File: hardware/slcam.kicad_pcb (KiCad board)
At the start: 4 copper layers, 42.2 x 25.4 mm, 34 parts, among them J1 532610671, J2 Conn_01x08, J3 Conn_01x04, J4 532610371, J5 532610371, U1 STM32F103C8Tx, U2 W25Q128JVS, U3 TCAN330G, U4 TPS2044D, Y1 Crystal_GND24

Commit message: hardware: finishing fixes and new components
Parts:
- added C10: 12pF, Capacitor_SMD:C_0603_1608Metric_Pad1.08x0.95mm_HandSolder, B.Cu at (234.1, 64.8)
- added C9: 12pF, Capacitor_SMD:C_0603_1608Metric_Pad1.08x0.95mm_HandSolder, B.Cu at (234.1, 62.6)
- added Y2: Crystal, lib:ECS-.327-12.5-34R-C-TR, B.Cu at (231.0, 63.7)
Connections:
- J1 pad 3: /SPI_MOSI -> /SPI_MISO
- J1 pad 4: /SPI_MISO -> /SPI2_MOSI
- J2 pad 2: /SPI_MOSI -> /SPI2_MOSI
- J2 pad 3: /SPI_MISO -> /SPI2_MISO
- J2 pad 4: /SPI_SCK -> /SPI2_SCK
- U1 pad 13: /SPI_NSS_FLASH -> unconnected-(U1-Pad13)
- U1 pad 23: unconnected-(U1-Pad23) -> GND
- U1 pad 25: unconnected-(U1-Pad25) -> /SPI_NSS_FLASH
- U1 pad 26: unconnected-(U1-Pad26) -> /SPI2_SCK
- U1 pad 27: unconnected-(U1-Pad27) -> /SPI2_MISO
- U1 pad 28: unconnected-(U1-Pad28) -> /SPI2_MOSI
- U1 pad 3: unconnected-(U1-Pad3) -> /OSC_IN2
- U1 pad 35: unconnected-(U1-Pad35) -> GND
- U1 pad 4: unconnected-(U1-Pad4) -> /OSC_OUT2
- U1 pad 40: unconnected-(U1-Pad40) -> /CAN_SHDN
- U1 pad 41: unconnected-(U1-Pad41) -> /CAN_S
- U1 pad 45: unconnected-(U1-Pad45) -> /FLASH_WP
- U1 pad 46: unconnected-(U1-Pad46) -> /FLASH_HR
- U1 pad 47: unconnected-(U1-Pad47) -> GND
- U1 pad 8: unconnected-(U1-Pad8) -> GND
- U2 pad 2: /SPI_MOSI -> /SPI2_MISO
- U2 pad 3: unconnected-(U2-Pad3) -> /FLASH_HR
- U2 pad 5: /SPI_MISO -> /SPI2_MOSI
- U2 pad 6: /SPI_SCK -> /SPI2_SCK
- U2 pad 7: unconnected-(U2-Pad7) -> /FLASH_WP
- U3 pad 5: unconnected-(U3-Pad5) -> /CAN_SHDN
- U3 pad 8: unconnected-(U3-Pad8) -> /CAN_S
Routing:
- net /SPI_MOSI: track 67.5 -> 0.00 mm, vias 1 -> 0
- net /SPI2_MISO: track 0.00 -> 62.9 mm
- net /SPI_MISO: track 63.1 -> 5.41 mm, vias 2 -> 1
- net /SPI_SCK: track 66.7 -> 12.0 mm, vias 3 -> 1
- net /SPI2_MOSI: track 0.00 -> 47.0 mm, vias 0 -> 3
- net /SPI2_SCK: track 0.00 -> 32.7 mm, vias 0 -> 2
- net GND: track 148.2 -> 170.0 mm, vias 13 -> 14
- net /CAN_S: track 0.00 -> 20.2 mm, vias 0 -> 2
- net /CAN_SHDN: track 0.00 -> 16.3 mm, vias 0 -> 2
- net /OSC_OUT2: track 0.00 -> 16.0 mm, vias 0 -> 2
- net /FLASH_HR: track 0.00 -> 15.6 mm, vias 0 -> 2
- net /OSC_IN2: track 0.00 -> 13.7 mm, vias 0 -> 2
- net /SPI_NSS_FLASH: track 23.7 -> 37.3 mm, vias 1 -> 2
- net /FLASH_WP: track 0.00 -> 11.2 mm, vias 0 -> 2
- net VCC: track 111.6 -> 114.6 mm
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
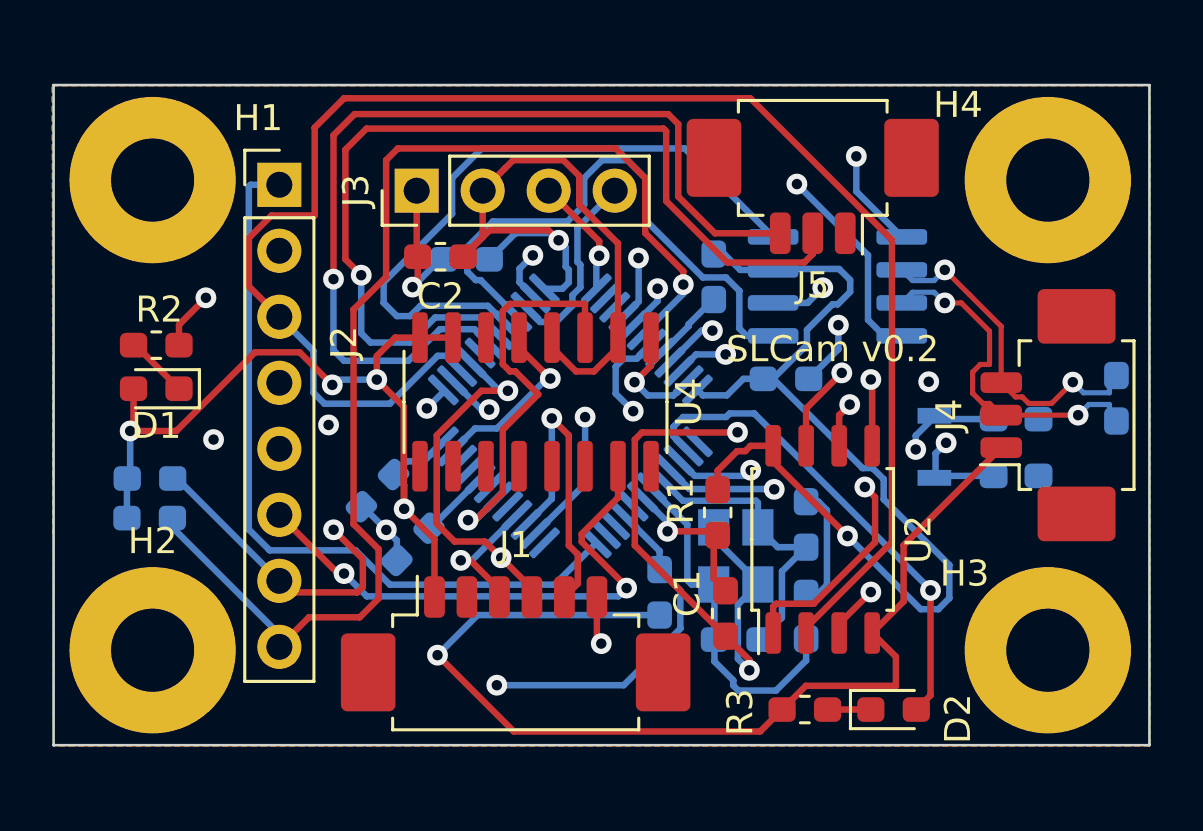
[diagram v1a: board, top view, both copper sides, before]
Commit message: hardware: Fixing DRC errors and general improvements in the layout
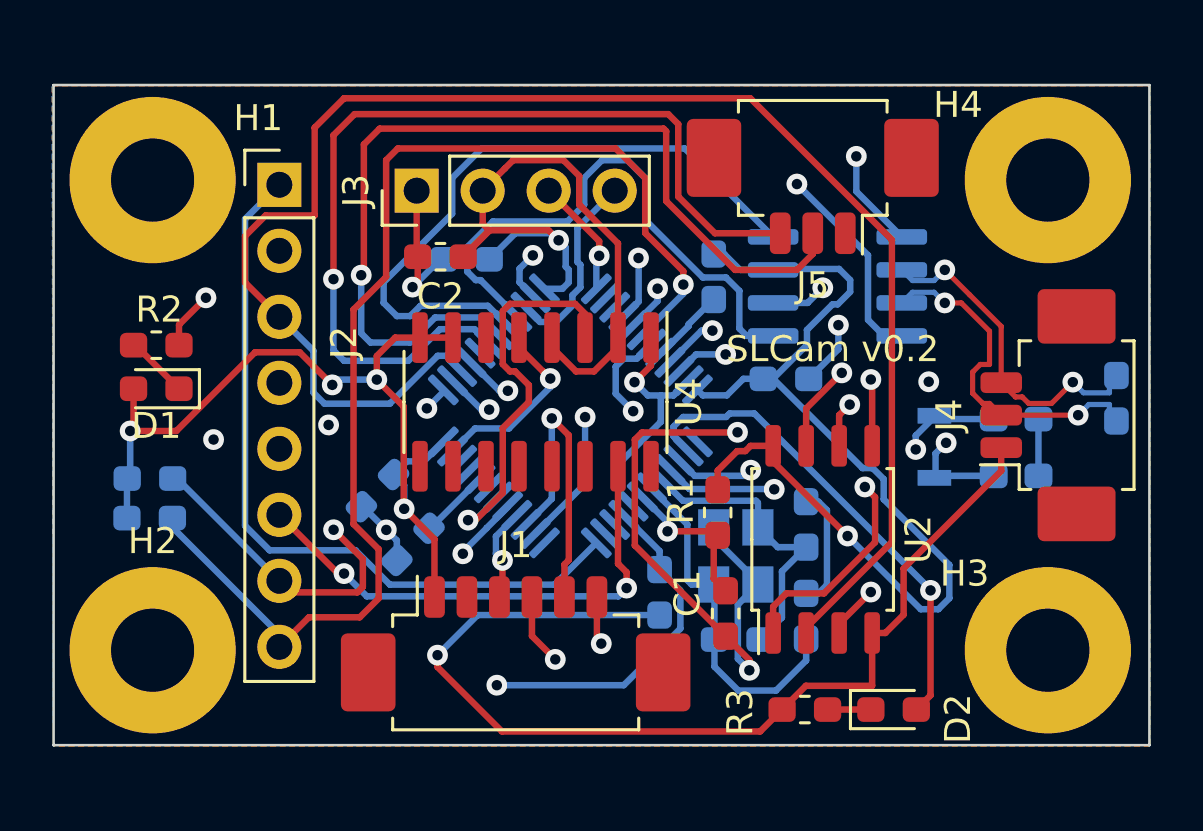
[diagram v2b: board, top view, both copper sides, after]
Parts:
- moved G*** 21.9 mm to (214.1, 72.4), turned to 180 degrees
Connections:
- J1 pad 4: /SPI2_MOSI -> /SPI_MOSI
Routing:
- net /SPI2_MOSI: track 47.0 -> 35.2 mm, vias 3 -> 2
- net /SPI_MOSI: track 0.00 -> 10.9 mm, vias 0 -> 2
- net GND: track 170.0 -> 177.0 mm
- net /SPI_MISO: track 5.41 -> 3.63 mm
- net /3V3_IMG_SENSOR: track 20.9 -> 19.7 mm
- net /SPI2_MISO: track 62.9 -> 61.8 mm
- net /UART_RX: track 36.4 -> 35.8 mm
- net /EN_SWITCH: track 16.1 -> 15.6 mm
- net /SPI_NSS_IMG: track 29.3 -> 28.8 mm

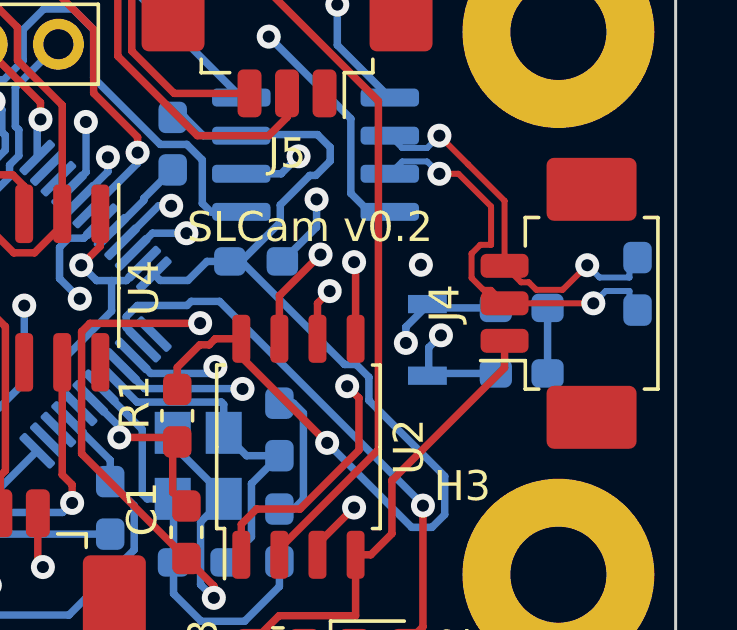
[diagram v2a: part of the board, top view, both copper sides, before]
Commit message: hardware: Fixing the footprint of the 32 kHz crystal #45
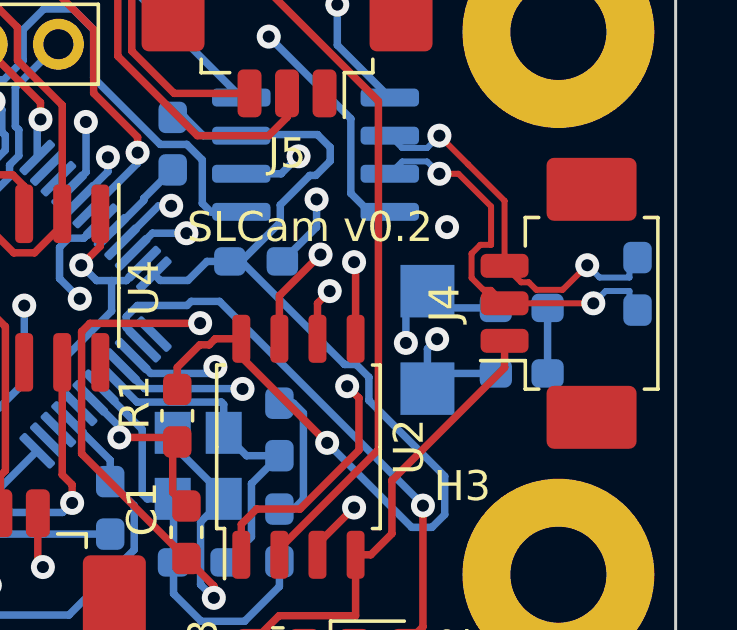
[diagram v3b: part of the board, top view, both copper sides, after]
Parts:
- Y2: footprint lib:ECS-.327-12.5-34R-C-TR -> Crystal:Crystal_SMD_MicroCrystal_CC7V-T1A-2Pin_3.2x1.5mm_HandSoldering
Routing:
- net /OSC_IN2: track 13.7 -> 14.3 mm

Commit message: hardware: changing component values #52
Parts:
- D1: value LED -> SMD Green LED
- D2: value LED -> SMD Orange LED
- U1: value STM32F103C8Tx -> STM32F103C8T6
- U3: value TCAN330G -> TCAN330GD
- U4: value TPS2044D -> TPS2010AD
- Y1: value Crystal_GND24 -> ECS-80-10-33-CHN-TR3
- Y2: value Crystal -> ECS-.327-12.5-34S-TR
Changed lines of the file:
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@@
       (effects (font (size 1 1) (thickness 0.15)))
     )
-    (fp_text value "TPS2044D" (at 0 5.9 90) (layer "F.Fab")
+    (fp_text value "TPS2010AD" (at 0 5.9 90) (layer "F.Fab")
       (effects (font (size 1 1) (thickness 0.15)))
     )
@@
       (effects (font (size 1 1) (thickness 0.15)))
     )
-    (fp_text value "LED" (at 0 1.43) (layer "F.Fab")
+    (fp_text value "SMD Green LED" (at 0 1.43) (layer "F.Fab")
       (effects (font (size 1 1) (thickness 0.15)))
     )
@@
       (effects (font (size 1 1) (thickness 0.15)))
     )
-    (fp_text value "LED" (at 0 1.43) (layer "F.Fab")
+    (fp_text value "SMD Orange LED" (at 0 1.43) (layer "F.Fab")
       (effects (font (size 1 1) (thickness 0.15)))
     )
@@
       (effects (font (size 1 1) (thickness 0.15)) (justify mirror))
     )
-    (fp_text value "STM32F103C8Tx" (at 0 -5.85 315) (layer "B.Fab")
+    (fp_text value "STM32F103C8T6" (at 0 -5.85 315) (layer "B.Fab")
       (effects (font (size 1 1) (thickness 0.15)) (justify mirror))
     )
@@
       (effects (font (size 1 1) (thickness 0.15)) (justify mirror))
     )
-    (fp_text value "Crystal_GND24" (at 0 -2.45 90) (layer "B.Fab")
+    (fp_text value "ECS-80-10-33-CHN-TR3" (at 0 -2.45 90) (layer "B.Fab")
       (effects (font (size 1 1) (thickness 0.15)) (justify mirror))
     )
@@
       (effects (font (size 1 1) (thickness 0.15)) (justify mirror))
     )
-    (fp_text value "TCAN330G" (at 0 -3.4) (layer "B.Fab")
+    (fp_text value "TCAN330GD" (at 0 -3.4) (layer "B.Fab")
       (effects (font (size 1 1) (thickness 0.15)) (justify mirror))
     )
@@
       (effects (font (size 1 1) (thickness 0.15)) (justify mirror))
     )
-    (fp_text value "Crystal" (at 0 -1.95 90) (layer "B.Fab")
+    (fp_text value "ECS-.327-12.5-34S-TR" (at 0 -1.95 90) (layer "B.Fab")
       (effects (font (size 1 1) (thickness 0.15)) (justify mirror))
     )
@@
     (pts (xy 239.268 49.784) (xy 239.268 75.184))
     (height -4.572)
-    (gr_text "25.4000 mm" (at 242.04 62.484 90) (layer "Dwgs.User")
+    (gr_text "25,4000 mm" (at 242.04 62.484 90) (layer "Dwgs.User")
       (effects (font (size 1.5 1.5) (thickness 0.3)))
     )
@@
     (pts (xy 197.104 75.184) (xy 239.268 75.184))
     (height 3.556)
-    (gr_text "42.1640 mm" (at 218.186 77.59) (layer "Dwgs.User")
-      (effects (font (size 1 1) (thickness 0.15)))
-    )
+    (gr_text "42,1640 mm" (at 218.186 77.59) (layer "Dwgs.User")
+      (effects (font (size 1 1) (thickness 0.15)))
+    )

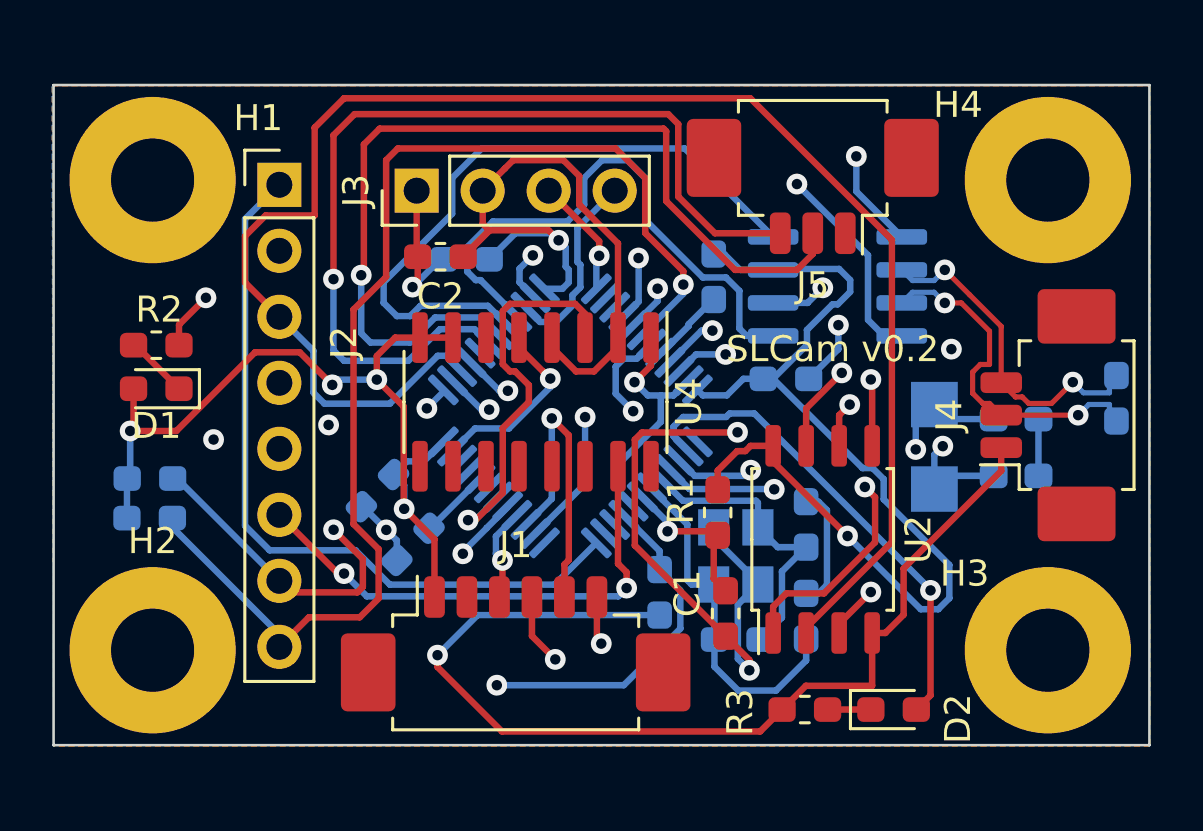
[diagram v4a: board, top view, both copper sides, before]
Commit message: hardware: fixing mouting holes
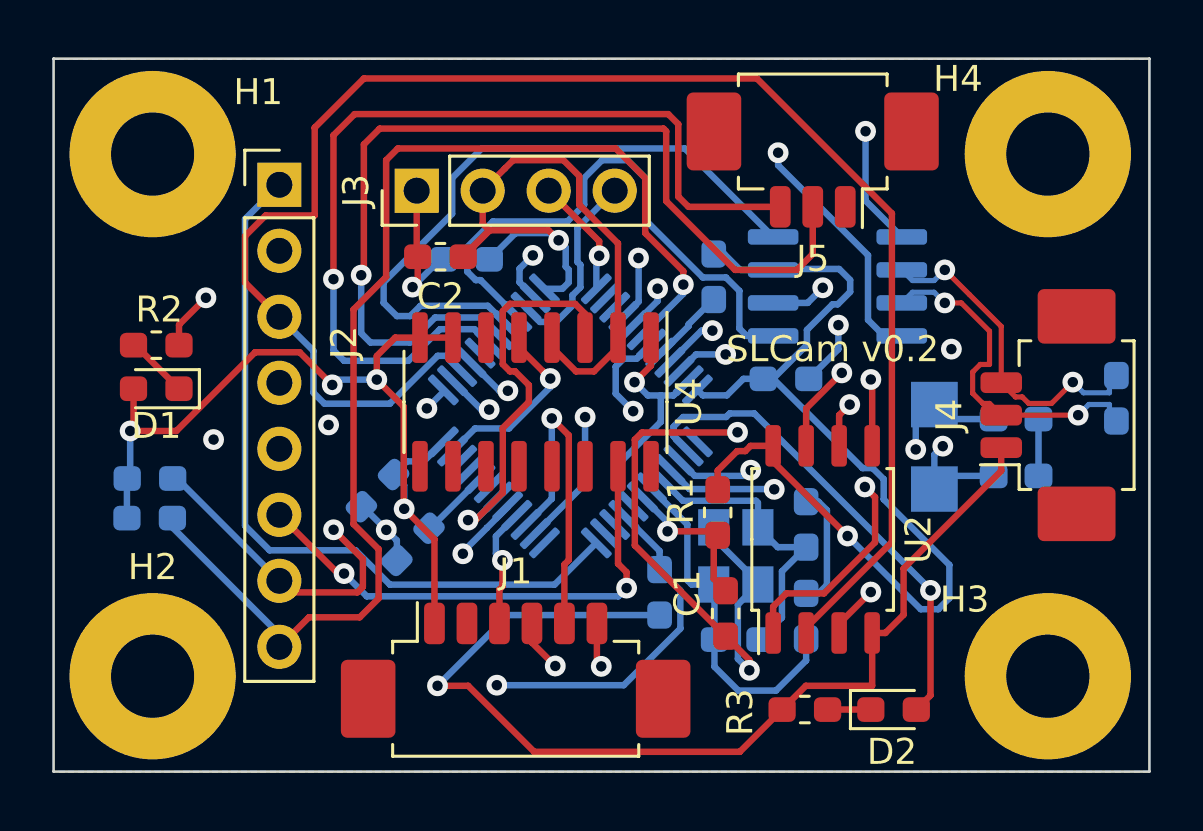
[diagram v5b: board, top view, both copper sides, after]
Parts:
- moved J5 1.02 mm to (226.3, 52.1)
- moved J1 1.02 mm to (214.9, 72.9)
- moved H1 1.00 mm to (200.9, 52.4)
- moved H2 1.00 mm to (200.9, 72.5)
- moved H3 1.00 mm to (235.4, 72.5)
- moved H4 1.00 mm to (235.4, 52.4)
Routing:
- net GND: track 177.4 -> 179.4 mm
- net /CAN_SHDN: track 16.3 -> 18.2 mm
- net /CAN_S: track 20.2 -> 21.4 mm
- net /SPI2_MISO: track 61.8 -> 63.1 mm
- net VCC: track 114.8 -> 115.8 mm
- net /SPI_SCK: track 11.7 -> 12.7 mm
- net /SPI_MISO: track 3.63 -> 4.65 mm
- net /UART_RX: track 35.8 -> 36.8 mm
- net /SPI_NSS: track 16.1 -> 16.9 mm
- net /SPI_MOSI: track 10.9 -> 10.3 mm
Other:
- board size 42.2 x 25.4 mm -> 42.2 x 27.4 mm

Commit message: hardware: layout: Minor fixes
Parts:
- D1: value SMD Green LED -> Green LED
- D2: value SMD Orange LED -> Orange LED
- J1: value 532610671 -> 53261-0671
- J4, J5: value 532610371 -> 53261-0371
- R2, R3: value 510 -> 510R
- R8: value 120 -> 120R
- U1: value STM32F103C8T6 -> STM32F103C8Tx
- U3: value TCAN330GD -> TCAN330G
- U4: value TPS2010AD -> TPS2044D
- Y1: value ECS-80-10-33-CHN-TR3 -> Crystal_GND24
- Y2: value ECS-.327-12.5-34S-TR -> Crystal
- moved G*** 1.78 mm to (214.1, 74.2)
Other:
- board text added: "42.1640 mm x 27.4320 mm"
- board text removed: "42.1640 mm x 25.4000 mm"

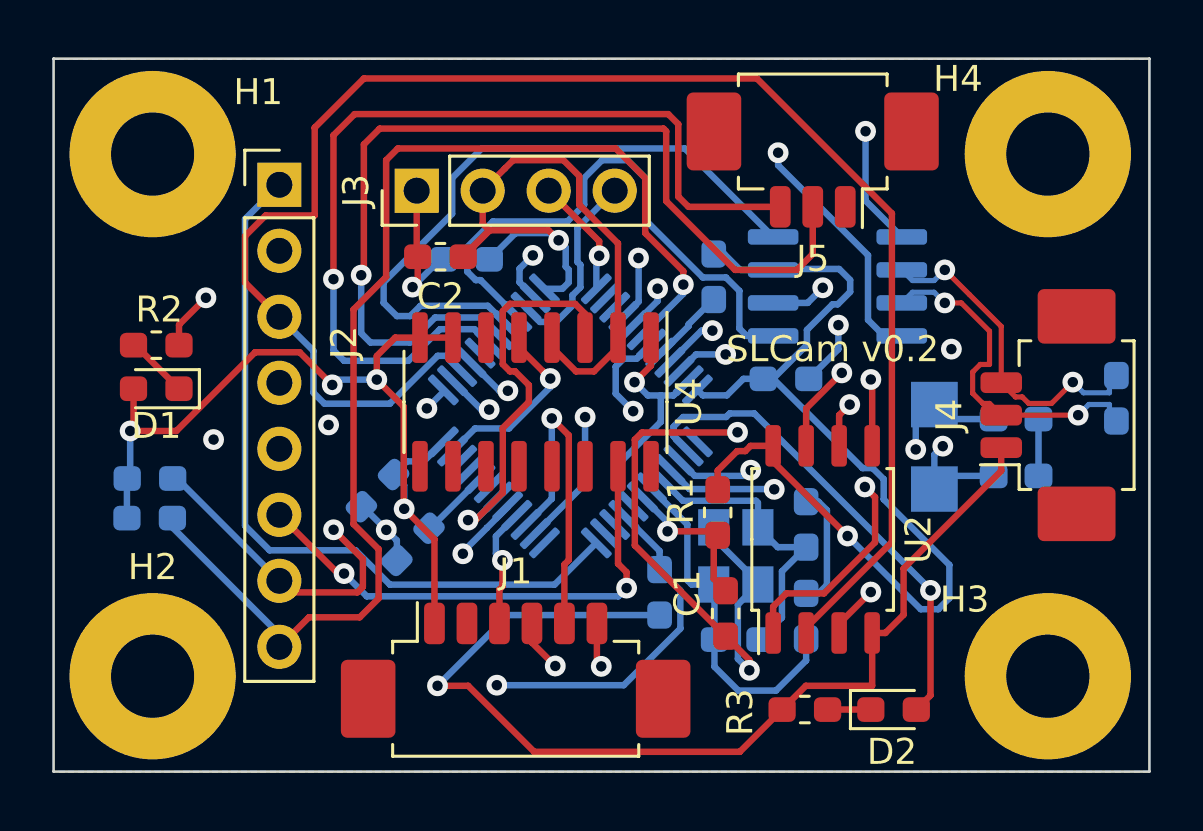
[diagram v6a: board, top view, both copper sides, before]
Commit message: hardware: fixing mounting holes
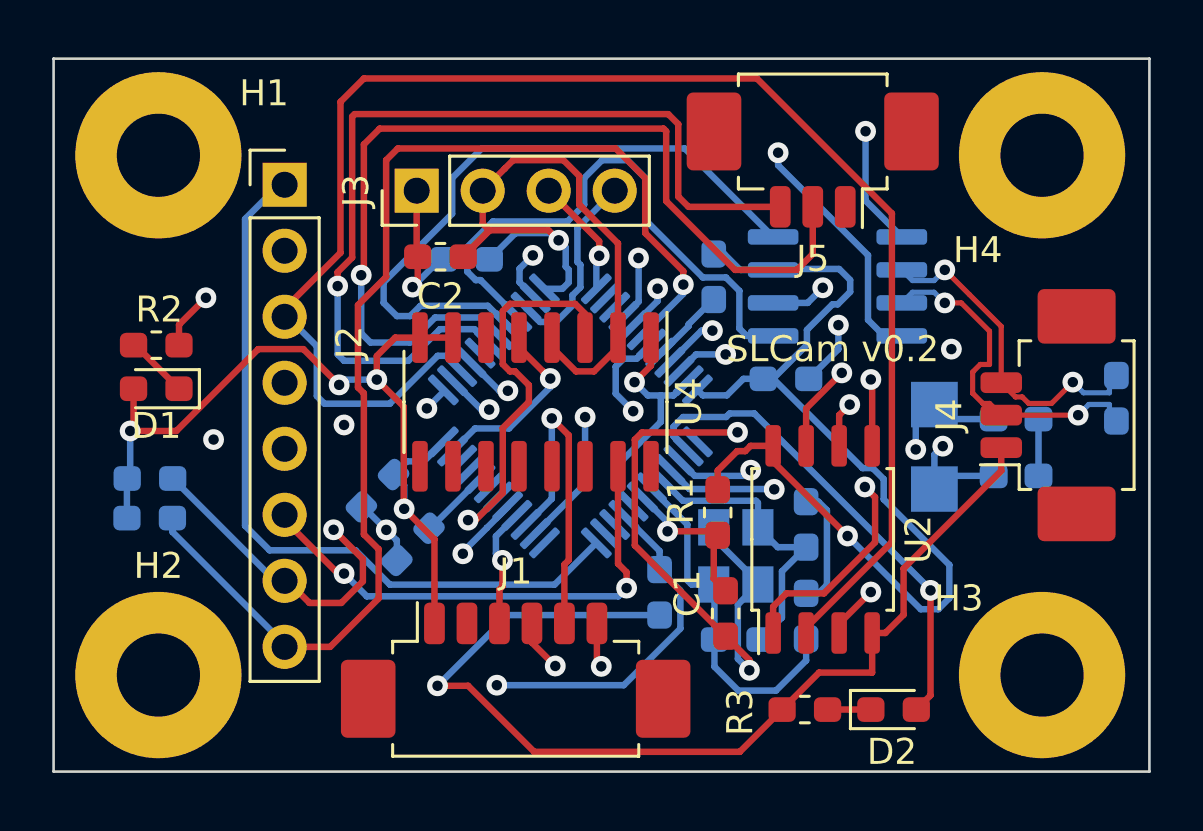
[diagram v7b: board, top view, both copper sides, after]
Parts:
- D1: value Green LED -> SMD Green LED
- D2: value Orange LED -> SMD Orange LED
- J1: value 53261-0671 -> 532610671
- J4, J5: value 53261-0371 -> 532610371
- R2, R3: value 510R -> 510
- R8: value 120R -> 120
- U1: value STM32F103C8Tx -> STM32F103C8T6
- U3: value TCAN330G -> TCAN330GD
- U4: value TPS2044D -> TPS2010AD
- Y1: value Crystal_GND24 -> ECS-80-10-33-CHN-TR3
- Y2: value Crystal -> ECS-.327-12.5-34S-TR
- moved G*** 1.78 mm to (214.1, 72.4)
- moved H1 0.23 mm to (201.1, 52.5)
- moved H2 0.23 mm to (201.1, 72.5)
- moved H3 0.23 mm to (235.1, 72.5)
- moved H4 0.23 mm to (235.1, 52.5)
- moved J2 0.20 mm to (206.0, 53.6)
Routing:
- net /SPI2_MISO: track 63.1 -> 60.6 mm
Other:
- board text added: "0,2000 mm / 0,0000 mm"
- board text added: "0,3000 mm"
- board text added: "1,6600 mm"
- board text added: "42,2640 mm x 27,5320 mm"
- board text removed: "0.2000 mm / 0.0000 mm"
- board text removed: "0.3000 mm"
- board text removed: "1.6600 mm"
- board text removed: "42.1640 mm x 27.4320 mm"
